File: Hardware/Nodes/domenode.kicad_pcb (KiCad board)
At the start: 2 copper layers, 100 x 70 mm, 83 parts, among them J1 MIC_JUMPER, J10 5V, J11 TOUCH, J12 24V, J13 CAN_BOARD, J15 RGB_SHIELD, J16 RGB_SHIELD, J17 GROVE/I2C, J18 ISP, J19 CAN_IN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

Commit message: Sorting power stage
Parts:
- added C15: 100nF, Capacitor_SMD:C_0603_1608Metric_Pad1.05x0.95mm_HandSolder, F.Cu at (146.2, 109.5)
- J19, J20: footprint RJ45:RJ45_GENERIC -> Connector_RJ:RJ45_Amphenol_RJHSE5380
- SW1, SW2, SW3, SW4: footprint Button_Switch_SMD:SW_SPST_B3S-1000 -> Button_Switch_SMD:SW_SPST_B3U-1000P
- moved J18 81.5 mm to (108.0, 124.8), turned to 90 degrees
- moved J3 76.5 mm to (108.0, 128.5), turned to 90 degrees
- moved R14 76.0 mm to (137.0, 128.8), turned to 90 degrees
- moved C10 74.6 mm to (143.8, 125.5), turned to 180 degrees
- moved R12 73.4 mm to (133.5, 128.8), turned to 270 degrees
- moved C7 63.8 mm to (136.1, 116.2), turned to 180 degrees
- moved C8 61.6 mm to (163.9, 109.5), turned to 180 degrees
- moved SW3 61.5 mm to (188.1, 95.0)
- moved C9 57.3 mm to (155.9, 116.2)
- moved SW4 56.2 mm to (188.1, 100.0)
- moved C12 53.8 mm to (128.8, 110.4), turned to 270 degrees
- moved C11 52.4 mm to (155.9, 103.0), turned to 180 degrees
- moved C13 47.5 mm to (135.9, 103.0), turned to 180 degrees
- moved C5 42.6 mm to (111.6, 95.0), turned to 180 degrees
- moved C4 42.4 mm to (112.0, 82.6)
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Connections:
- J18 pad 1: VCC -> CANGND
- J18 pad 2: TX -> RX
- J18 pad 3: RX -> TX
- J18 pad 4: CANGND -> VCC
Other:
- board text added: "Node:"

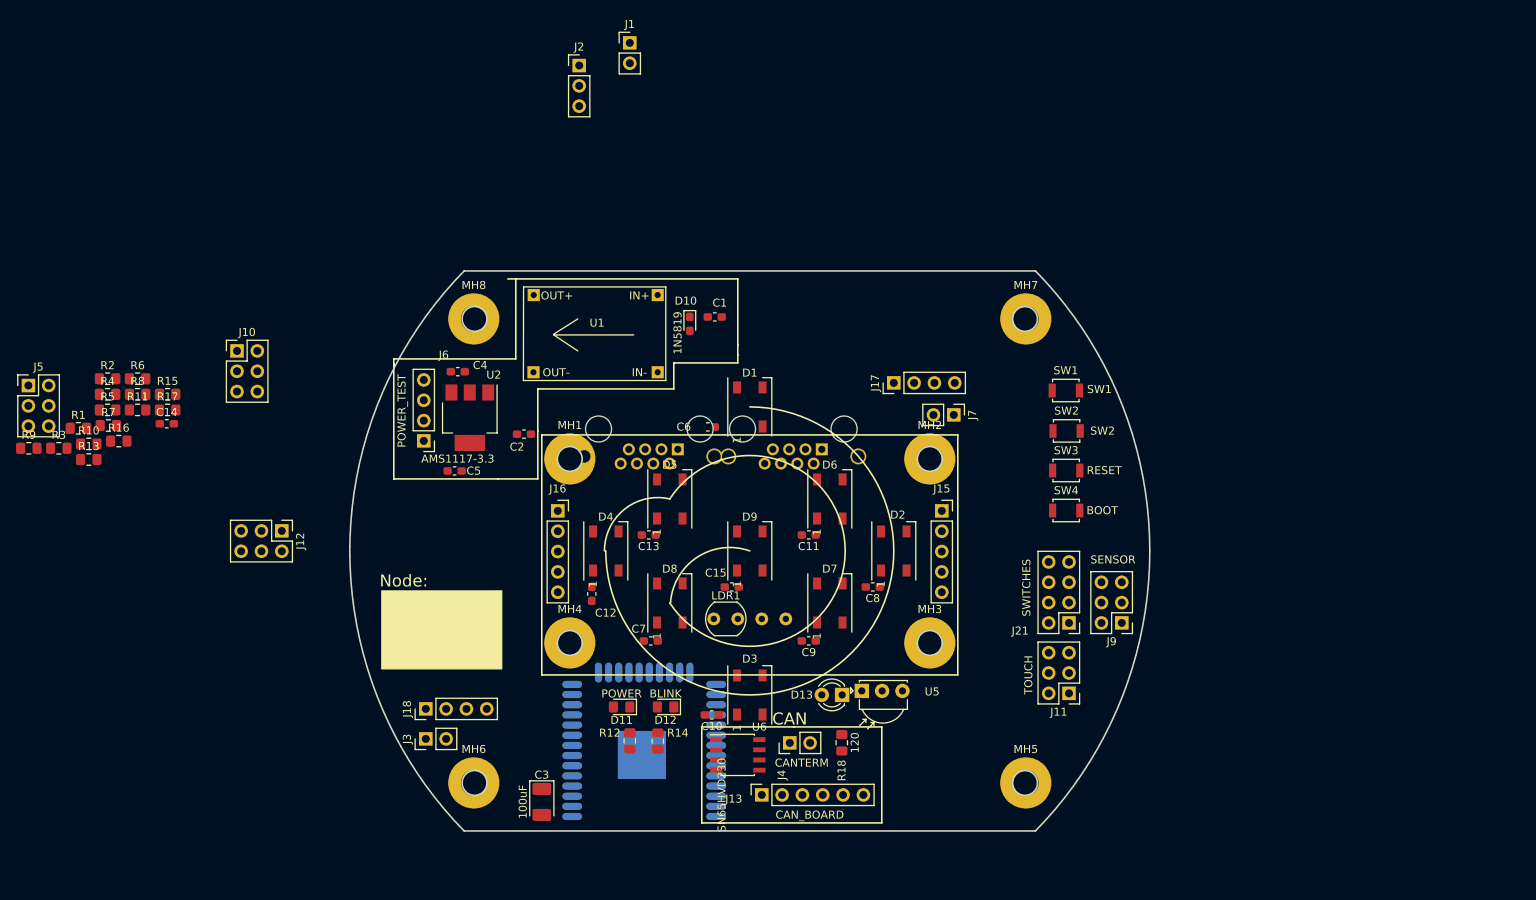
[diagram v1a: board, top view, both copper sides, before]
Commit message: More wiring and layout
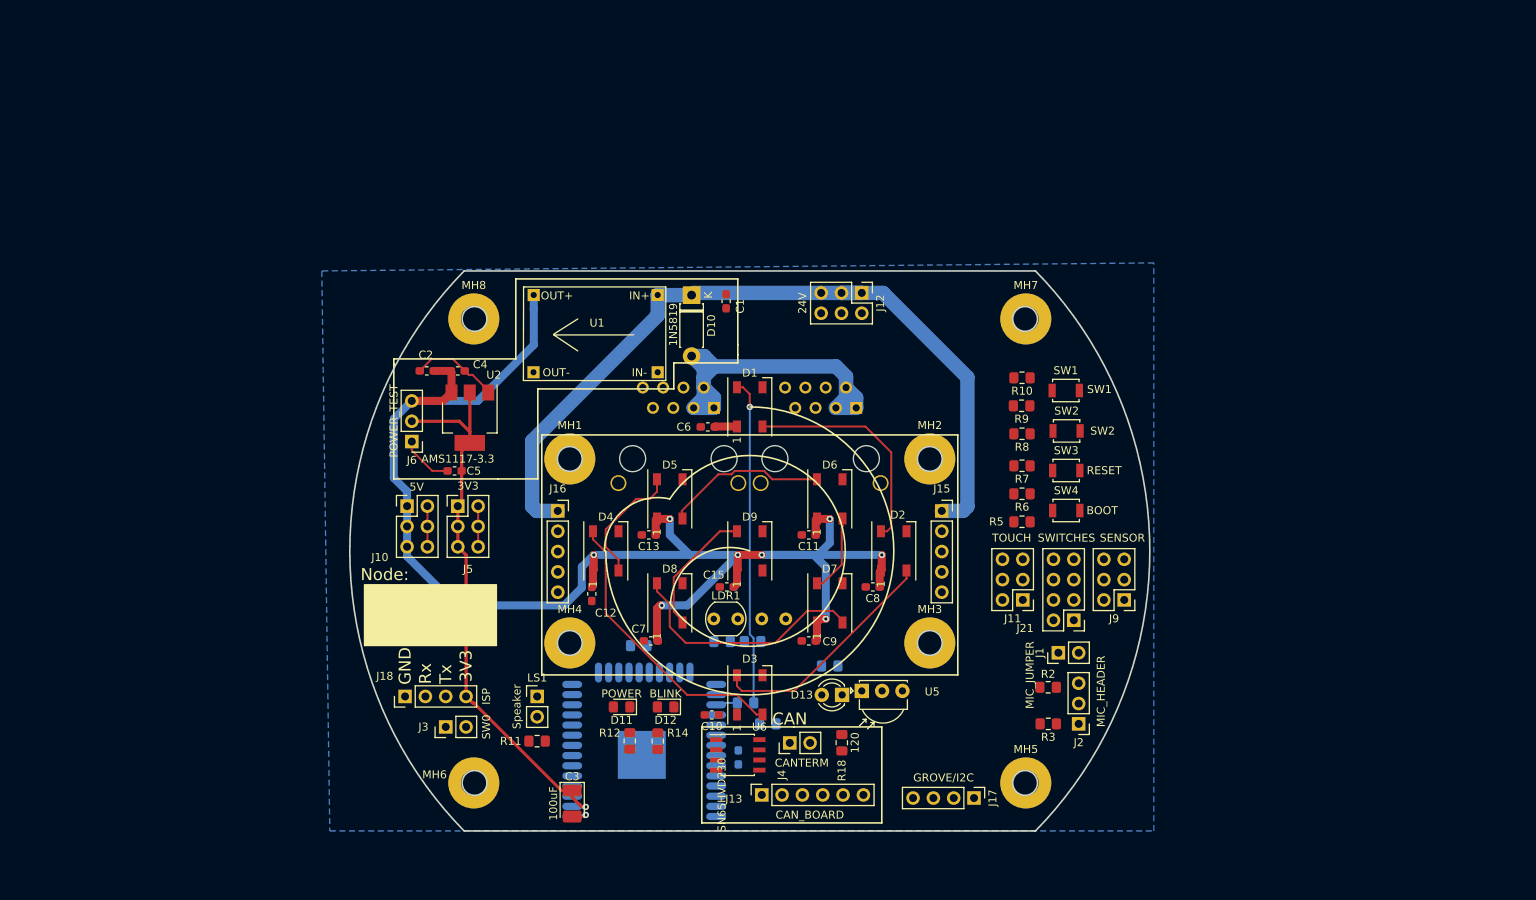
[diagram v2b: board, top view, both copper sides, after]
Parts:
- removed J7: SPEAKER, Connector_PinHeader_2.54mm:PinHeader_1x02_P2.54mm_Vertical
- added LS1: Speaker, Connector_PinHeader_2.54mm:PinHeader_1x02_P2.54mm_Vertical, F.Cu at (121.9, 123.2)
- C14, R1, R13, R15, R16, R17, R4: moved to B.Cu
- D10: footprint Diode_SMD:D_0603_1608Metric_Pad1.05x0.95mm_HandSolder -> Diode_THT:D_DO-41_SOD81_P7.62mm_Horizontal
- J19, J20: footprint Connector_RJ:RJ45_Amphenol_RJHSE5380 -> RJ45:RJ45_GENERIC
- J6: footprint Connector_PinHeader_2.54mm:PinHeader_1x04_P2.54mm_Vertical -> Connector_PinHeader_2.54mm:PinHeader_1x03_P2.54mm_Vertical
- moved R3 128.4 mm to (185.8, 126.6), turned to 180 degrees
- moved R9 124.2 mm to (182.5, 86.9), turned to 180 degrees
- moved R2 123.7 mm to (185.8, 122.0)
- moved R10 116.9 mm to (182.5, 83.4), turned to 180 degrees
- moved R5 115.2 mm to (182.5, 101.4), turned to 180 degrees
- moved R7 114.3 mm to (182.5, 94.4), turned to 180 degrees
- moved R6 111.5 mm to (182.5, 97.9), turned to 180 degrees
- moved R8 110.7 mm to (182.5, 90.4), turned to 180 degrees
- moved J2 103.3 mm to (189.6, 126.6), turned to 180 degrees
- moved R16 93.2 mm to (158.5, 119.4), turned to 180 degrees
- moved J1 93.2 mm to (187.1, 117.7), turned to 90 degrees
- moved R13 87.6 mm to (148.0, 124.0), turned to 180 degrees
- moved R4 86.3 mm to (148.8, 116.3)
- moved R1 84.8 mm to (145.0, 116.3), turned to 180 degrees
- moved R17 84.7 mm to (150.7, 126.6)
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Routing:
- net +5V: track 0.00 -> 190.5 mm, vias 0 -> 8
- net +24V: track 0.00 -> 101.8 mm
- net VCC: track 0.00 -> 69.7 mm, vias 0 -> 1
- net CANV: track 0.00 -> 46.9 mm
- net Net-(D1-Pad4): track 0.00 -> 40.8 mm, vias 0 -> 1
- net Net-(D3-Pad2): track 0.00 -> 35.8 mm
- net CANGND: track 0.00 -> 31.4 mm, vias 0 -> 1
- net Net-(D7-Pad2): track 0.00 -> 30.9 mm
- net Net-(D2-Pad2): track 0.00 -> 29.6 mm
- net Net-(D1-Pad2): track 0.00 -> 28.3 mm
- net Net-(D5-Pad2): track 0.00 -> 20.4 mm
- net Net-(D8-Pad2): track 0.00 -> 16.4 mm
- net Net-(D4-Pad2): track 0.00 -> 15.7 mm
- net Net-(D6-Pad2): track 0.00 -> 9.86 mm
- net PIXELS: track 0.00 -> 2.75 mm
- added copper zone on B.Cu, net CANGND
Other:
- net class 24V added: clearance 0.6, trace_width 1.8, via_dia 0.8, via_drill 0.4
- net class 5V added: clearance 0.3, trace_width 1, via_dia 0.8, via_drill 0.4
- net class VCC added: clearance 0.2, trace_width 0.4, via_dia 0.8, via_drill 0.4
- board text added: "3V3"
- board text added: "GND"
- board text added: "Rx"
- board text added: "Tx"

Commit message: moved some stuff around and it's looking potentially better
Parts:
- moved R10 71.6 mm to (131.5, 133.5)
- moved SW3 69.8 mm to (132.0, 136.5)
- moved J17 63.7 mm to (114.8, 120.2), turned to 0 degrees
- moved SW4 61.2 mm to (139.0, 136.5)
- moved J13 60.4 mm to (210.0, 128.2)
- moved J4 60.4 mm to (213.5, 121.8)
- moved R18 60.4 mm to (220.0, 121.7)
- moved U6 60.4 mm to (207.0, 123.2)
- moved R17 59.2 mm to (209.8, 122.2), turned to 270 degrees
- moved C14 57.7 mm to (204.2, 123.4)
- moved R5 54.5 mm to (138.5, 133.5)
- moved J18 45.5 mm to (150.6, 128.9), turned to 0 degrees
- moved J3 43.7 mm to (154.0, 123.2), turned to 180 degrees
- moved R13 19.0 mm to (148.5, 105.0), turned to 270 degrees
- moved U5 2.55 mm to (165.0, 122.0)
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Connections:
- R13 pad 1: Net-(D1-Pad4) -> Net-(D9-Pad2)
- U3 pad 12: RLDR -> SW4
- U3 pad 16: FLDR -> SW3
- U3 pad 6: SW3 -> FLDR
- U3 pad 7: SW4 -> RLDR
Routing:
- net +5V: track 190.5 -> 246.1 mm, vias 8 -> 1
- net CANL: track 0.00 -> 45.3 mm
- net RED: track 0.00 -> 44.1 mm
- net GREEN: track 0.00 -> 43.1 mm
- net CANH: track 0.00 -> 42.6 mm
- net BLUE: track 0.00 -> 41.8 mm
- net Net-(D1-Pad4): track 40.8 -> 0.75 mm, vias 1 -> 0
- net PIXELS: track 2.75 -> 21.9 mm
- net CTX: track 0.00 -> 18.2 mm
- net CRX: track 0.00 -> 16.4 mm
- net SW0: track 0.00 -> 14.0 mm
- net VP: track 0.00 -> 8.96 mm
- net Net-(J4-Pad1): track 0.00 -> 8.10 mm
- net EN: track 0.00 -> 7.62 mm, vias 0 -> 1
- net RX: track 0.00 -> 6.95 mm
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
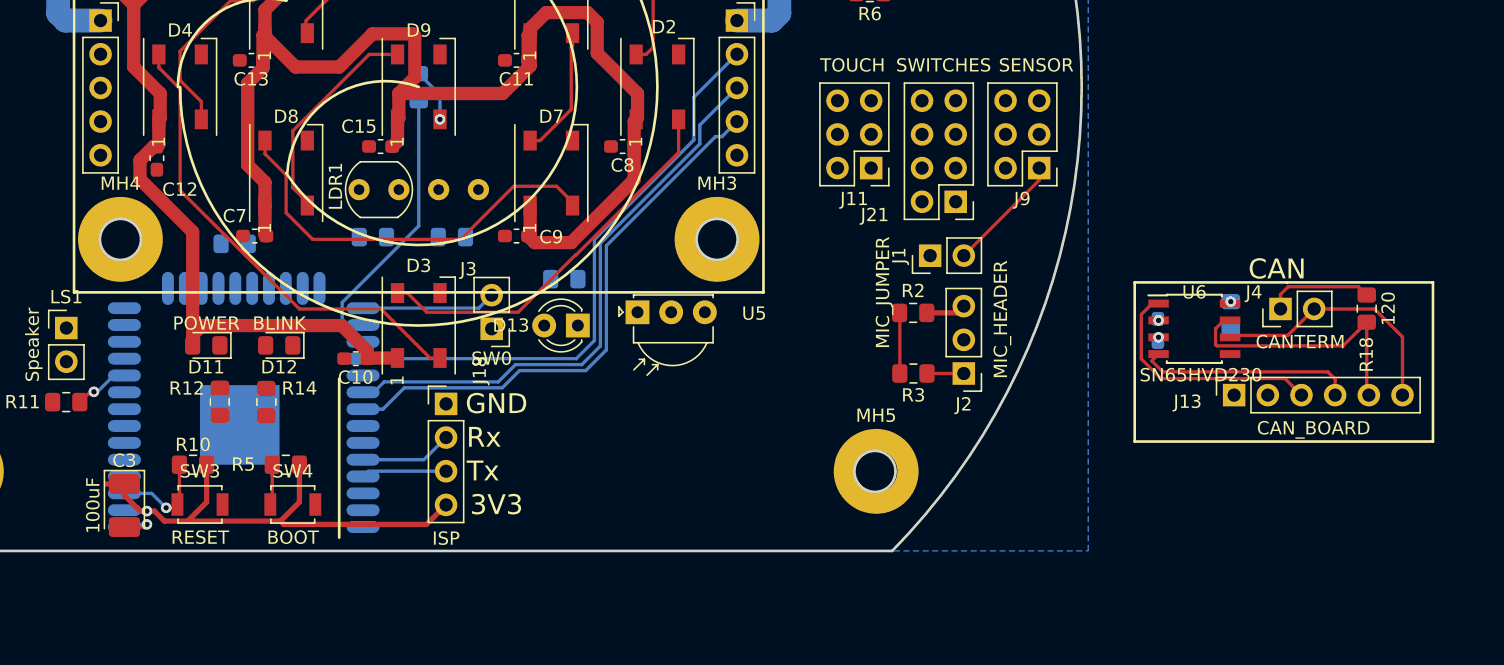
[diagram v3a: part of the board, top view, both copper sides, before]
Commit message: More PCB work. Added footprint for IR transistor (MMBT2222A)
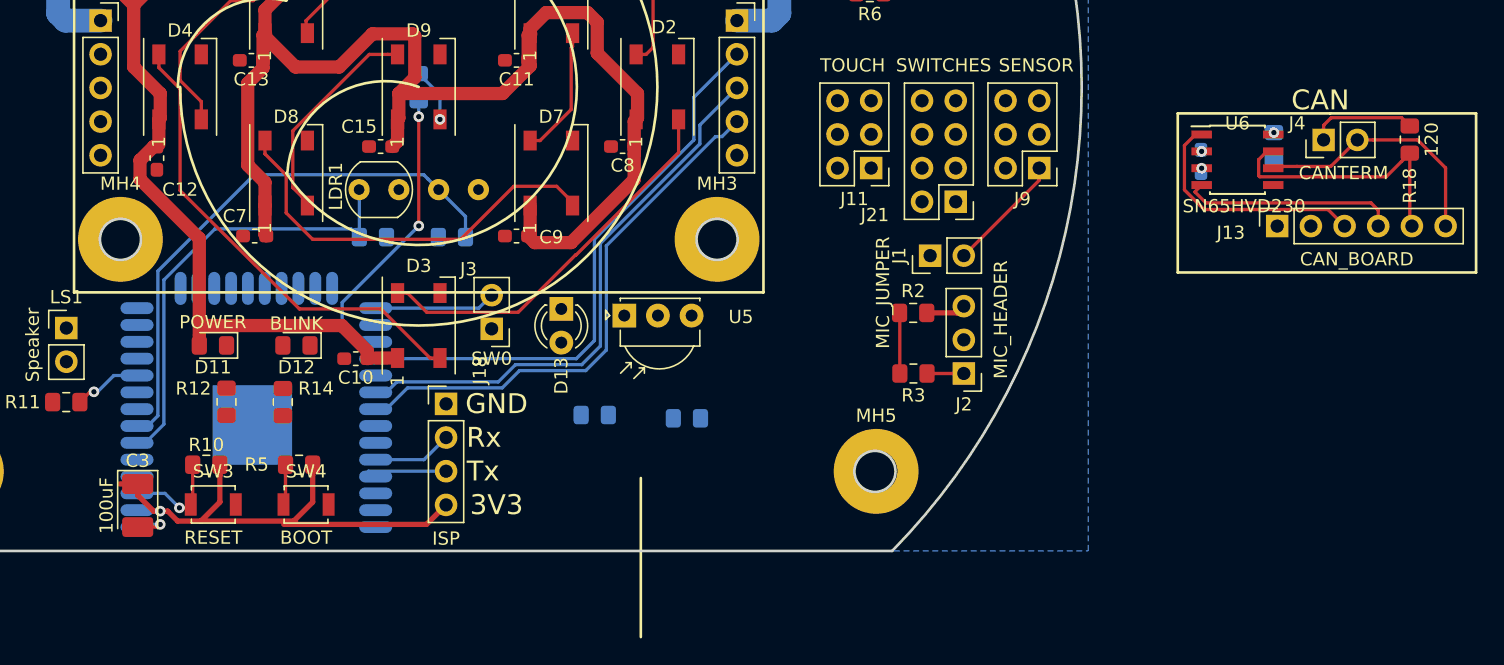
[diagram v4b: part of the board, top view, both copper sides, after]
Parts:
- moved R15 30.1 mm to (161.8, 129.8)
- moved R16 14.0 mm to (168.7, 130.0)
- moved C14 13.2 mm to (207.5, 110.6)
- moved J13 13.2 mm to (213.2, 115.5)
- moved J4 13.2 mm to (216.8, 109.0)
- moved R17 13.2 mm to (213.0, 109.5)
- moved R18 13.2 mm to (223.2, 109.0)
- moved U6 13.2 mm to (210.2, 110.5)
- moved D13 1.77 mm to (159.2, 121.8), turned to 270 degrees
- moved D12 1.30 mm to (139.3, 124.5)
- moved R14 1.25 mm to (138.2, 128.8)
- moved U5 1.03 mm to (164.0, 122.2)
- moved C3 1.00 mm to (127.3, 136.6)
- moved R10 1.00 mm to (132.5, 133.5)
- moved R5 1.00 mm to (139.5, 133.5)
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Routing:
- net RLDR: track 0.00 -> 42.5 mm
- net FLDR: track 0.00 -> 34.3 mm
- net +5V: track 246.1 -> 245.1 mm
- net BLUE: track 41.8 -> 42.3 mm
- net PIXELS: vias 0 -> 2
